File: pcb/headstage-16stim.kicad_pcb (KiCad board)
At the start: 6 copper layers, 40 x 51 mm, 132 parts, among them J1 OE_COAX-ADAPTER-XFL-A (DNP), J2 DF40C-70DP-0.4V(51), J3 SBH11-PBPC-D05-ST-BK, J5 PINHD-1x7_ONIXJTAG-RevA, SW1 R-668049, U1 RHS2116, U10 NCP163AFCT120T2G, U11 W25Q80EWUXIE, U12 DSC6011JI1A-050.0000, U13 TPS826951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

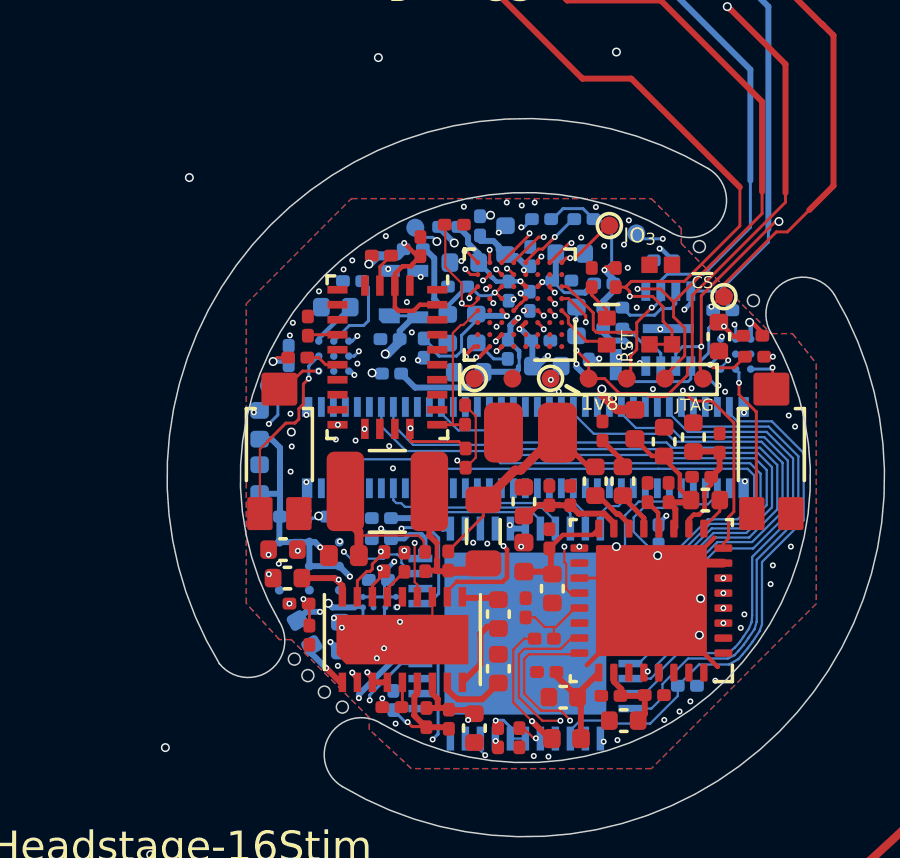
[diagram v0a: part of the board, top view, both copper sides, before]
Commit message: PCB Revision A
- Added production files from Speedy
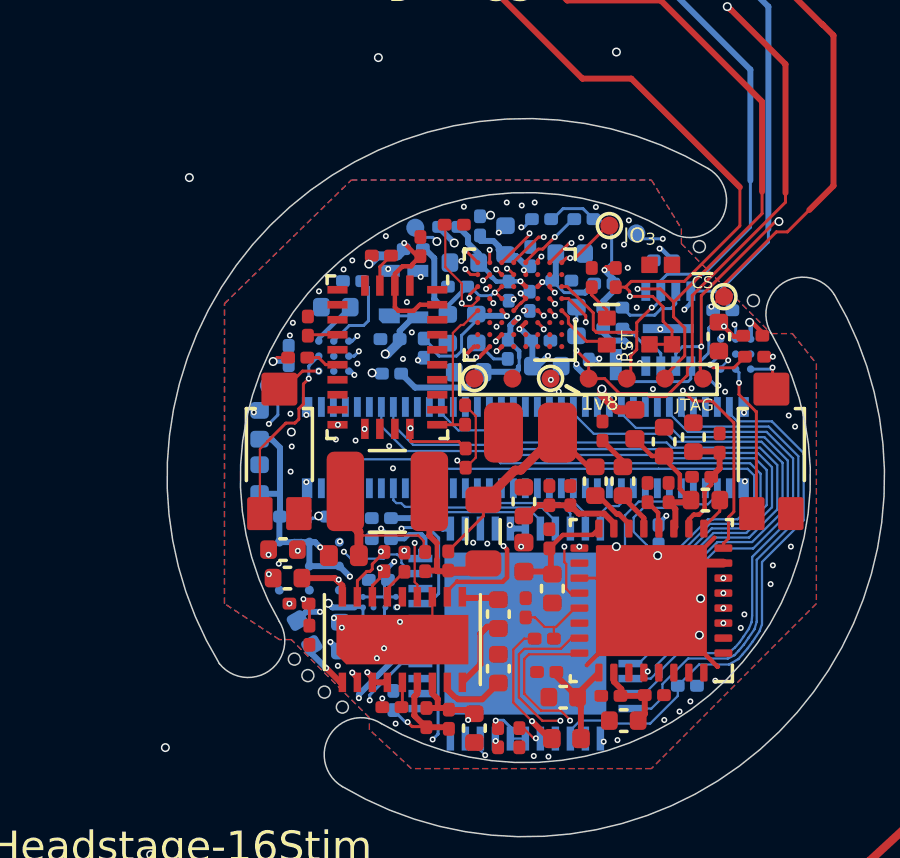
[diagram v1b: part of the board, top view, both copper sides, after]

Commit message: Revision B
- Bring in changes from headstage-rhs116 rev. C that should make this design
  fully functional
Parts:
- removed ?: , jonnew-eagle:OE-LOGO-7X5
- removed the G*** at (123.7, 54.3)
- removed SW1: R-668049, jonnew:MITSUMI_R-668049
- added R5: 124k,1%, Resistor_SMD:R_0201_0603Metric, F.Cu at (131.3, 67.3)
- added R6: 124k,1%, Resistor_SMD:R_0201_0603Metric, F.Cu at (131.3, 65.9)
- added TP5: GPIO2, jonnew:TestPoint_Pad_D0.6mm, F.Cu at (124.0, 54.2)
- R19, R23: value 125k,1% -> 124k,1%
- R3: value 39.2,1% -> 39.2k,1%
- moved G*** 10.8 mm to (127.8, 55.5)
- moved C4 0.07 mm to (127.8, 70.3)
- moved C1 0.07 mm to (126.7, 71.1)
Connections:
- U7 pad 18: unconnected-(U7-Pad18) -> /Serializer/GPIO1
- U7 pad 27: unconnected-(U7-Pad27) -> /FPGA/GPIO2_{Ser}
- U8 pad C3: /FPGA/TDI -> /FPGA/CRESET_{B}
- U8 pad E3: unconnected-(U8-PadE3) -> /FPGA/TDI
- U8 pad G1: unconnected-(U8-PadG1) -> /FPGA/GPIO2_{Ser}
- U9 pad B1: +4V -> /DC Tap & Regulation/3v3_{EN}
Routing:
- net /DC Tap & Regulation/3v3_{EN}: track 0.00 -> 26.5 mm, vias 0 -> 2
- net /FPGA/GPIO2_{Ser}: track 0.00 -> 25.2 mm, vias 0 -> 4
- net +7V: track 16.0 -> 26.7 mm, vias 4 -> 5
- net +1V8: track 91.0 -> 88.2 mm
- net /FPGA/CRESET_{B}: track 30.4 -> 28.6 mm, vias 2 -> 3
- net /FPGA/TDI: track 41.6 -> 43.3 mm
- net GND: track 24.0 -> 25.6 mm, vias 104 -> 111
- net /FPGA/DI_{Flash}/TMS: track 33.9 -> 34.6 mm
- net /FPGA/CLK_{Ser}: track 15.9 -> 15.3 mm
- net /FPGA/GPIO0_{Ser}: track 23.6 -> 23.0 mm
- net /3D Pose/PD_{0}+: track 6.24 -> 5.65 mm
- net Net-(F1-Pad1): track 5.55 -> 5.02 mm
- net +2V5: track 20.0 -> 20.5 mm
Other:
- board size 40 x 51 mm -> 40 x 56 mm
- board text added: "HS-16Stim Rev.B '24"
- board text added: "IO_{2}"
- board text added: "JPN, Open Ephys Inc. '24"
- board text added: "ONIX Headstage-16Stim Board Rev. B"
- board text added: "rB"
- board text removed: "HS-16Stim Rev.A '22"
- board text removed: "Headstage-16Stim Rev. A JPN '22"
- board text removed: "RST"
